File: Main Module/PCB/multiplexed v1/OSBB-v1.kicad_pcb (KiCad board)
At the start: 2 copper layers, 85.6 x 49.8 mm, 42 parts, among them P1 AUX 1-3, P14 EXTRA Pins, P2 Wire to Teensy VUSB, P3 +3.3V, P4 Pit Limiter, P5 Encoders, P6 BTN 1-32, Q1 NPN, Q2 NPN, Q3 NPN, Q4 NPN, U1 74HC4051, U2 74HC4051, U3 74HC4051, U4 74HC4051, U5 Teensy3.2

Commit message: * RC5-dev joined missing ground traces for right side of board
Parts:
- removed the REF** at (190.8, 121.5)
- removed the REF** at (243.7, 125.5)
- P4: value Pit Limiter -> Pit
- moved C6 5.32 mm to (210.7, 125.9), turned to 270 degrees
- moved REF** 0.08 mm to (180.4, 121.7)
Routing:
- net Net-(R2-Pad1): track 20.1 -> 22.7 mm
- net GND: track 311.3 -> 313.4 mm, vias 7 -> 8
- net +3V3: track 311.1 -> 311.9 mm, vias 8 -> 10
- net Net-(R7-Pad1): track 25.2 -> 25.3 mm, vias 1 -> 2
- net Net-(U1-Pad3): vias 1 -> 0

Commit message: * PCB RC5-dev labels
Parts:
- removed the G*** at (179.6, 126.6)
- added G***: LOGO, MOBB-KiCad-Lib:OPEN_HW_LOGO_3MM, F.Cu at (179.8, 126.5)
- added REF***: OSHW-Logo_5.7x6mm_Copper, Symbols:OSHW-Logo_5.7x6mm_Copper, B.Cu at (181.1, 127.6)
- moved Q1 0.60 mm to (195.6, 140.5)
- moved Q2 0.58 mm to (201.2, 140.5)
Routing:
- net Net-(U4-Pad3): track 28.7 -> 26.5 mm, vias 3 -> 4
- net Net-(P6-Pad57): track 20.3 -> 19.0 mm
- net Net-(P1-Pad5): track 16.4 -> 17.5 mm
- net GND: track 313.4 -> 314.2 mm
- net Net-(P1-Pad1): track 24.7 -> 24.0 mm
- net Net-(P1-Pad3): track 14.2 -> 13.6 mm
- net Net-(Q2-Pad2): track 24.7 -> 24.1 mm
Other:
- board text added: "(c) 2016 Mirko Kaiser"
- board text added: "+"
- board text added: "-"
- board text added: "32"

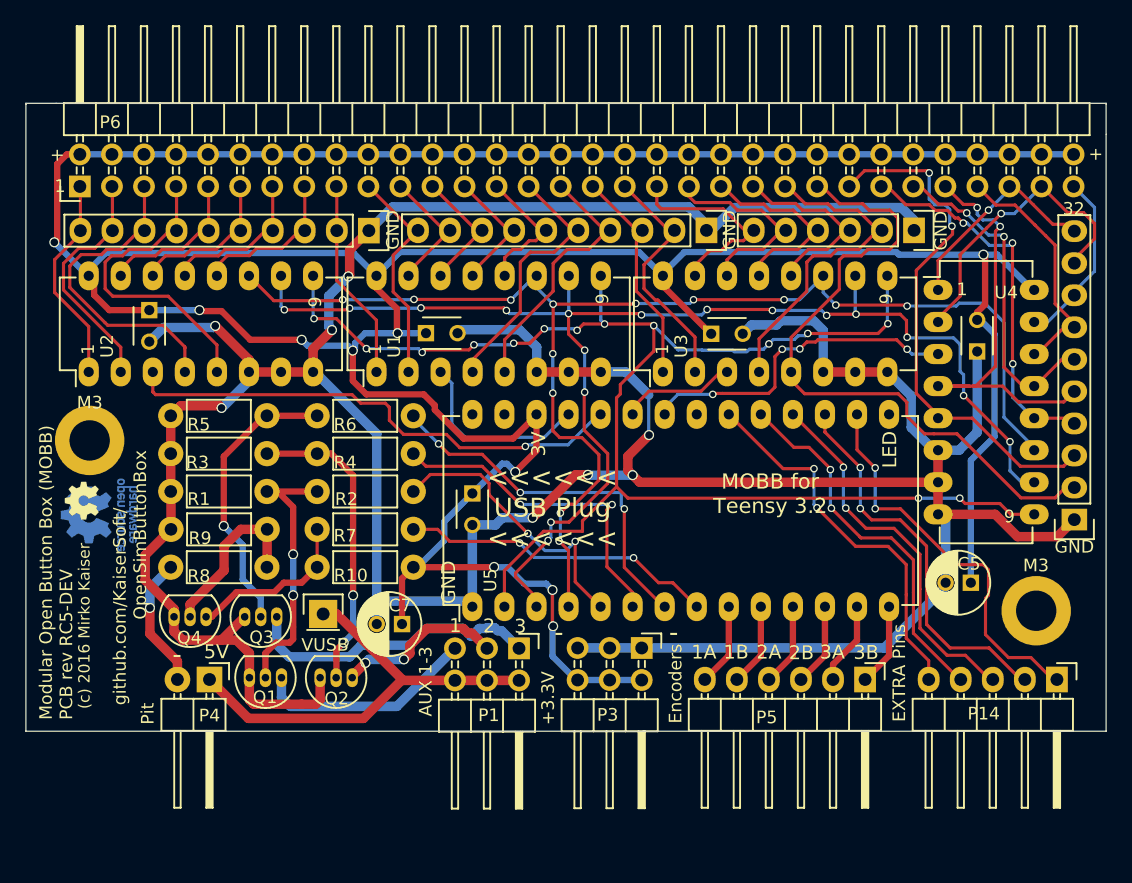
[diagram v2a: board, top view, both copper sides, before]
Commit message: * changed orientation of cap to give more room around screw * adjusted distance between lower pins (aux, 3v...) * more labels
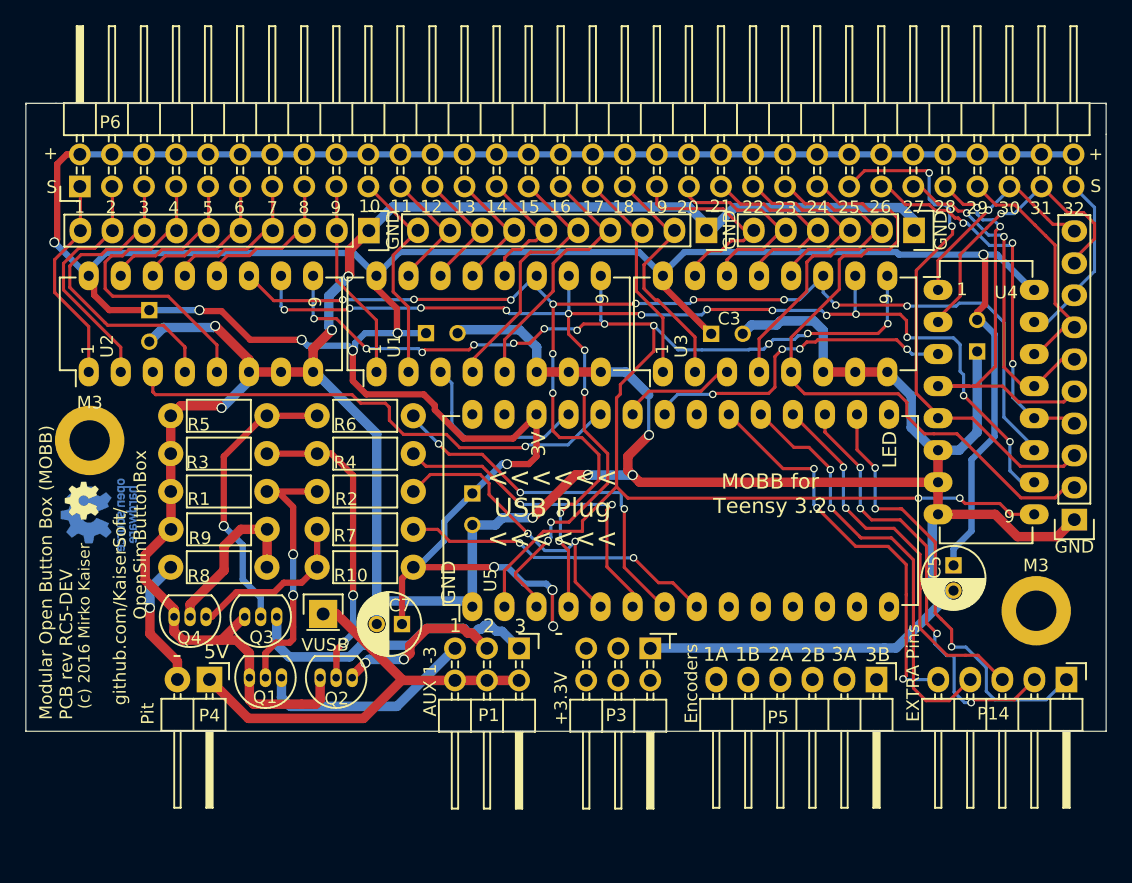
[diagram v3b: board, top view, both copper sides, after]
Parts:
- C1, C2, C3, C4, C6: moved to B.Cu
- moved C5 1.94 mm to (248.8, 131.6), turned to 270 degrees
- moved P5 0.91 mm to (242.7, 140.7)
- moved P14 0.76 mm to (257.8, 140.7)
- moved P3 0.68 mm to (224.8, 138.2)
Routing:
- net +3V3: track 311.9 -> 300.7 mm
- net Net-(P5-Pad6): track 6.56 -> 0.00 mm
- net Net-(P5-Pad5): track 6.56 -> 0.00 mm
- net Net-(P5-Pad4): track 6.56 -> 0.00 mm
- net Net-(P5-Pad1): track 6.56 -> 0.00 mm
- net Net-(P5-Pad2): track 6.56 -> 0.00 mm
- net Net-(P5-Pad3): track 6.56 -> 0.00 mm
- net Net-(P14-Pad4): track 29.7 -> 34.4 mm
- net Net-(P14-Pad2): track 30.9 -> 35.5 mm, vias 2 -> 4
- net GND: track 314.2 -> 310.2 mm
- net Net-(P14-Pad1): track 31.8 -> 35.7 mm, vias 2 -> 3
- net Net-(P14-Pad5): track 30.8 -> 33.0 mm, vias 2 -> 3
- net Net-(P14-Pad3): track 29.9 -> 30.6 mm
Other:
- board text added: "10"
- board text added: "11"
- board text added: "12"
- board text added: "13"
- board text added: "14"
- board text added: "15"
- board text added: "16"
- board text added: "17"
- board text added: "18"
- board text added: "19"
- board text added: "20"
- board text added: "21"
- board text added: "22"
- board text added: "23"
- board text added: "24"
- board text added: "25"
- board text added: "26"
- board text added: "27"
- board text added: "28"
- board text added: "29"
- board text added: "30"
- board text added: "31"
- board text added: "4"
- board text added: "5"
- board text added: "6"
- board text added: "7"
- board text added: "8"
- board text added: "S"

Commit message: * fixed missing tracks from last release
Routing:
- net +3V3: track 300.7 -> 311.8 mm
- net Net-(P5-Pad6): track 0.00 -> 6.19 mm
- net Net-(P5-Pad5): track 0.00 -> 6.19 mm
- net Net-(P5-Pad4): track 0.00 -> 6.19 mm
- net Net-(P5-Pad2): track 0.00 -> 6.19 mm
- net Net-(P5-Pad1): track 0.00 -> 6.19 mm
- net Net-(P5-Pad3): track 0.00 -> 6.19 mm
- net GND: track 310.2 -> 315.6 mm
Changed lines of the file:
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@@
   (general
     (links 194)
-    (no_connects 11)
+    (no_connects 0)
     (area 175.269999 88.074999 261.407144 151.803575)
     (thickness 1.6)
     (drawings 97)
-    (tracks 1131)
+    (tracks 1158)
     (zones 0)
     (modules 41)
@@
   (segment (start 195.575 142.1) (end 195.575 140.525) (width 0.75) (layer B.Cu) (net 4))
   (segment (start 196.275 142.8) (end 195.575 142.1) (width 0.75) (layer B.Cu) (net 4))
-  (segment (start 217.1 136.45) (end 217.2 136.45) (width 0.5) (layer B.Cu) (net 5))
+  (segment (start 222.26 140.74) (end 224.8 140.74) (width 0.5) (layer B.Cu) (net 5) (status C00000))
+  (segment (start 219.72 140.74) (end 222.26 140.74) (width 0.5) (layer B.Cu) (net 5) (status C00000))
+  (segment (start 217.1 136.45) (end 217.1 139.3) (width 0.5) (layer B.Cu) (net 5))
   (via (at 217.1 136.45) (size 0.8) (drill 0.6) (layers F.Cu B.Cu) (net 5))
+  (segment (start 217.2 136.45) (end 217.1 136.45) (width 0.5) (layer B.Cu) (net 5))
+  (segment (start 218.54 140.74) (end 219.72 140.74) (width 0.5) (layer B.Cu) (net 5) (status 800000))
+  (segment (start 217.1 139.3) (end 218.54 140.74) (width 0.5) (layer B.Cu) (net 5))
   (segment (start 250.25 123.25) (end 252.075 121.425) (width 0.5) (layer B.Cu) (net 5))
   (segment (start 252.075 113.3) (end 252.075 121.425) (width 0.5) (layer B.Cu) (net 5))
@@
   (segment (start 255.8 99.06) (end 253.26 99.06) (width 0.5) (layer B.Cu) (net 5))
   (segment (start 258.61 99.06) (end 258.34 99.06) (width 0.5) (layer B.Cu) (net 5))
-  (segment (start 225.08 138.17) (end 243.33 138.17) (width 0.75) (layer B.Cu) (net 6))
+  (segment (start 222.26 138.2) (end 219.72 138.2) (width 0.75) (layer B.Cu) (net 6) (status C00000))
+  (segment (start 224.8 138.2) (end 222.26 138.2) (width 0.75) (layer B.Cu) (net 6) (status C00000))
+  (segment (start 243.35 138.17) (end 224.83 138.17) (width 0.75) (layer B.Cu) (net 6) (status 800000))
+  (segment (start 224.83 138.17) (end 224.8 138.2) (width 0.75) (layer B.Cu) (net 6) (status C00000))
   (segment (start 244.28 138.17) (end 248.825 133.625) (width 0.75) (layer B.Cu) (net 6))
-  (segment (start 243.33 138.17) (end 244.28 138.17) (width 0.75) (layer B.Cu) (net 6))
+  (segment (start 243.33 138.17) (end 243.35 138.17) (width 0.75) (layer B.Cu) (net 6))
+  (segment (start 243.35 138.17) (end 244.28 138.17) (width 0.75) (layer B.Cu) (net 6))
   (segment (start 225.08 138.17) (end 225.05 138.2) (width 0.75) (layer B.Cu) (net 6))
   (segment (start 248.825 133.625) (end 247.875 133.625) (width 0.75) (layer B.Cu) (net 6))
@@
   (segment (start 185.15 137.05) (end 187.33 139.23) (width 0.75) (layer F.Cu) (net 7))
   (segment (start 187.33 139.23) (end 187.33 140.67) (width 0.75) (layer F.Cu) (net 7))
+  (segment (start 243.72 134.9) (end 243.72 137.605) (width 0.5) (layer F.Cu) (net 8) (status 400000))
+  (segment (start 242.725 138.6) (end 242.725 140.675) (width 0.5) (layer F.Cu) (net 8) (status 800000))
+  (segment (start 243.72 137.605) (end 242.725 138.6) (width 0.5) (layer F.Cu) (net 8))
+  (segment (start 241.18 134.9) (end 241.18 137.195) (width 0.5) (layer F.Cu) (net 9) (status 400000))
+  (segment (start 240.185 138.19) (end 240.185 140.675) (width 0.5) (layer F.Cu) (net 9) (status 800000))
+  (segment (start 241.18 137.195) (end 240.185 138.19) (width 0.5) (layer F.Cu) (net 9))
+  (segment (start 238.64 134.9) (end 238.64 137.635) (width 0.5) (layer F.Cu) (net 10) (status 400000))
+  (segment (start 237.645 138.63) (end 237.645 140.675) (width 0.5) (layer F.Cu) (net 10) (status 800000))
+  (segment (start 238.64 137.635) (end 237.645 138.63) (width 0.5) (layer F.Cu) (net 10))
+  (segment (start 236.1 134.9) (end 236.1 137.85) (width 0.5) (layer F.Cu) (net 11) (status 400000))
+  (segment (start 235.105 138.845) (end 235.105 140.675) (width 0.5) (layer F.Cu) (net 11) (status 800000))
+  (segment (start 236.1 137.85) (end 235.105 138.845) (width 0.5) (layer F.Cu) (net 11))
+  (segment (start 233.56 134.9) (end 233.56 138.04) (width 0.5) (layer F.Cu) (net 12) (status 400000))
+  (segment (start 232.565 139.035) (end 232.565 140.675) (width 0.5) (layer F.Cu) (net 12) (status 800000))
+  (segment (start 233.56 138.04) (end 232.565 139.035) (width 0.5) (layer F.Cu) (net 12))
+  (segment (start 231.02 134.9) (end 231.02 138.13) (width 0.5) (layer F.Cu) (net 13) (status 400000))
+  (segment (start 230.025 139.125) (end 230.025 140.675) (width 0.5) (layer F.Cu) (net 13) (status 800000))
+  (segment (start 231.02 138.13) (end 230.025 139.125) (width 0.5) (layer F.Cu) (net 13))
   (segment (start 179.64 105.1) (end 179.64 101.64) (width 0.25) (layer F.Cu) (net 14))
   (segment (start 179.64 101.64) (end 179.6 101.6) (width 0.25) (layer F.Cu) (net 14))

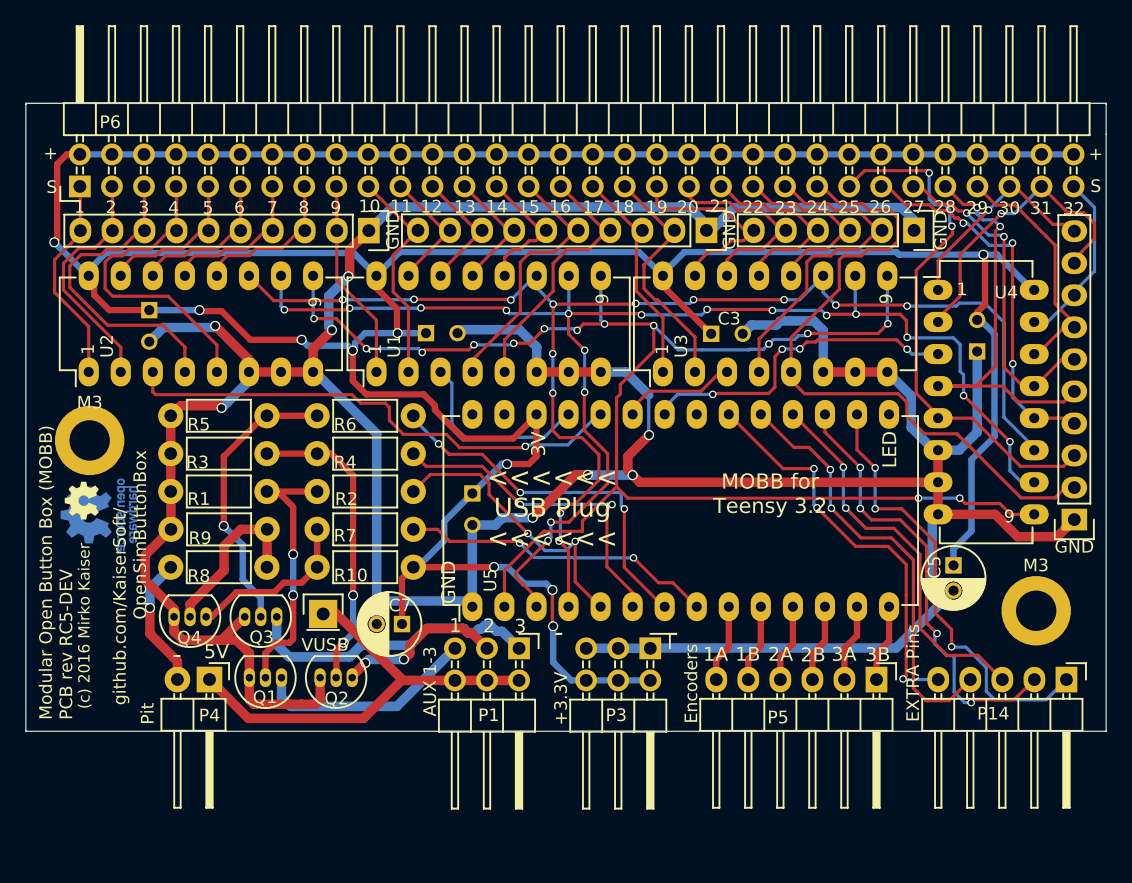
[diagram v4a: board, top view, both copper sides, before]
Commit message: * flooded with GND * added vias
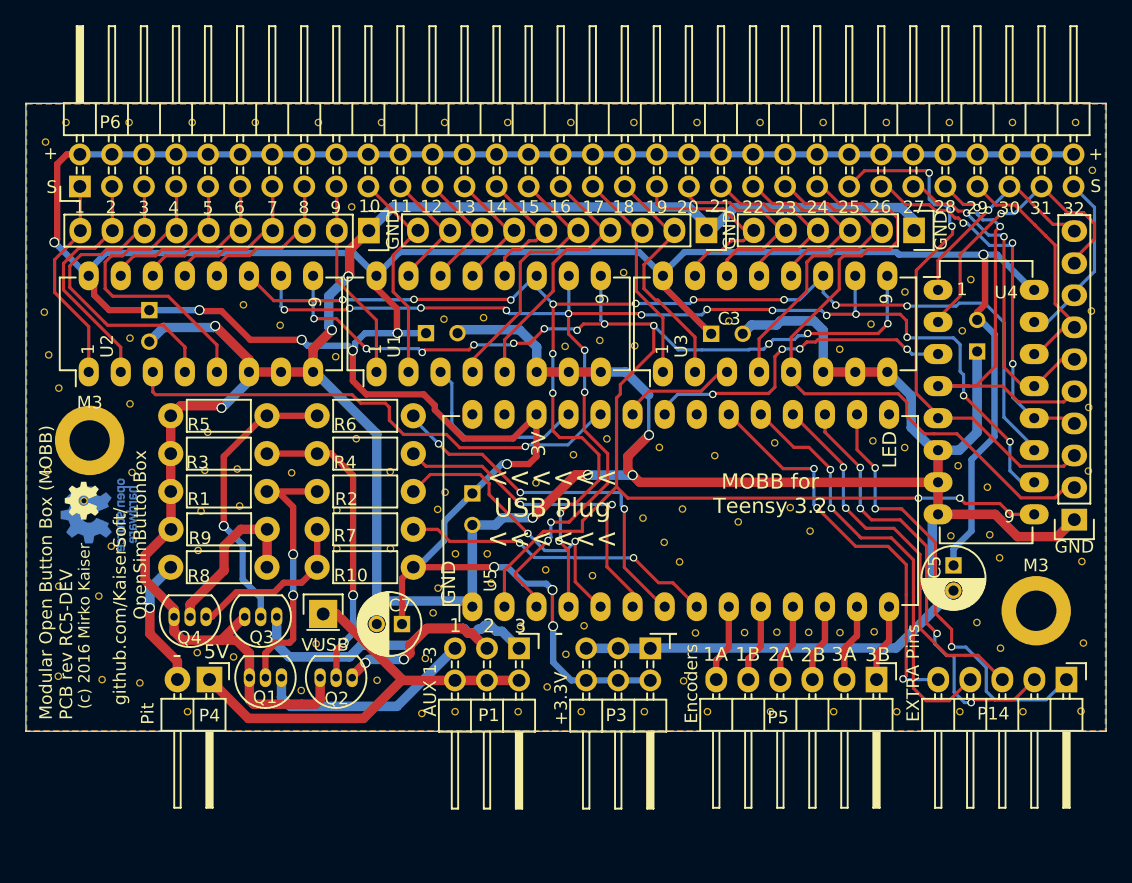
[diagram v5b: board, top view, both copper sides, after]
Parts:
- added Ref**: Val**, MOBB-KiCad-Lib:VIA-W0.6mm-H0.4mm, F.Cu at (258.9, 143.2)
- added Ref**: Val**, MOBB-KiCad-Lib:VIA-W0.6mm-H0.4mm, F.Cu at (214.3, 143.2)
- added Ref**: Val**, MOBB-KiCad-Lib:VIA-W0.6mm-H0.4mm, F.Cu at (184.3, 140.9)
- added Ref**: Val**, MOBB-KiCad-Lib:VIA-W0.6mm-H0.4mm, F.Cu at (188.1, 143.2)
- added Ref**: Val**, MOBB-KiCad-Lib:VIA-W0.6mm-H0.4mm, F.Cu at (188.9, 138.5)
- added Ref**: Val**, MOBB-KiCad-Lib:VIA-W0.6mm-H0.4mm, F.Cu at (191.8, 138.9)
- added Ref**: Val**, MOBB-KiCad-Lib:VIA-W0.6mm-H0.4mm, F.Cu at (198.3, 137.8)
- added Ref**: Val**, MOBB-KiCad-Lib:VIA-W0.6mm-H0.4mm, F.Cu at (197.1, 141.5)
- added Ref**: Val**, MOBB-KiCad-Lib:VIA-W0.6mm-H0.4mm, F.Cu at (206.7, 143.4)
- added Ref**: Val**, MOBB-KiCad-Lib:VIA-W0.6mm-H0.4mm, F.Cu at (209.3, 143.2)
- added Ref**: Val**, MOBB-KiCad-Lib:VIA-W0.6mm-H0.4mm, F.Cu at (214.5, 136.4)
- added Ref**: Val**, MOBB-KiCad-Lib:VIA-W0.6mm-H0.4mm, F.Cu at (219.6, 136.4)
- added Ref**: Val**, MOBB-KiCad-Lib:VIA-W0.6mm-H0.4mm, F.Cu at (178.5, 96.5)
- added Ref**: Val**, MOBB-KiCad-Lib:VIA-W0.6mm-H0.4mm, F.Cu at (218.1, 138.7)
- added Ref**: Val**, MOBB-KiCad-Lib:VIA-W0.6mm-H0.4mm, F.Cu at (216.6, 141.3)
- added Ref**: Val**, MOBB-KiCad-Lib:VIA-W0.6mm-H0.4mm, F.Cu at (228.4, 137.0)
- added Ref**: Val**, MOBB-KiCad-Lib:VIA-W0.6mm-H0.4mm, F.Cu at (227.4, 140.8)
- added Ref**: Val**, MOBB-KiCad-Lib:VIA-W0.6mm-H0.4mm, F.Cu at (252.6, 138.2)
- added Ref**: Val**, MOBB-KiCad-Lib:VIA-W0.6mm-H0.4mm, F.Cu at (250.7, 136.2)
- added Ref**: Val**, MOBB-KiCad-Lib:VIA-W0.6mm-H0.4mm, F.Cu at (259.1, 137.8)
- added Ref**: Val**, MOBB-KiCad-Lib:VIA-W0.6mm-H0.4mm, F.Cu at (259.0, 131.3)
- added Ref**: Val**, MOBB-KiCad-Lib:VIA-W0.6mm-H0.4mm, F.Cu at (252.5, 131.0)
- added Ref**: Val**, MOBB-KiCad-Lib:VIA-W0.6mm-H0.4mm, F.Cu at (251.7, 129.2)
- added Ref**: Val**, MOBB-KiCad-Lib:VIA-W0.6mm-H0.4mm, F.Cu at (183.5, 96.5)
- added Ref**: Val**, MOBB-KiCad-Lib:VIA-W0.6mm-H0.4mm, F.Cu at (248.6, 129.3)
- added Ref**: Val**, MOBB-KiCad-Lib:VIA-W0.6mm-H0.4mm, F.Cu at (235.9, 127.0)
- added Ref**: Val**, MOBB-KiCad-Lib:VIA-W0.6mm-H0.4mm, F.Cu at (237.5, 128.9)
- added Ref**: Val**, MOBB-KiCad-Lib:VIA-W0.6mm-H0.4mm, F.Cu at (231.8, 128.2)
- added Ref**: Val**, MOBB-KiCad-Lib:VIA-W0.6mm-H0.4mm, F.Cu at (227.3, 127.2)
- added Ref**: Val**, MOBB-KiCad-Lib:VIA-W0.6mm-H0.4mm, F.Cu at (227.1, 131.3)
- added Ref**: Val**, MOBB-KiCad-Lib:VIA-W0.6mm-H0.4mm, F.Cu at (225.9, 129.8)
- added Ref**: Val**, MOBB-KiCad-Lib:VIA-W0.6mm-H0.4mm, F.Cu at (224.2, 127.9)
- added Ref**: Val**, MOBB-KiCad-Lib:VIA-W0.6mm-H0.4mm, F.Cu at (188.5, 96.5)
- added Ref**: Val**, MOBB-KiCad-Lib:VIA-W0.6mm-H0.4mm, F.Cu at (193.5, 96.5)
- added Ref**: Val**, MOBB-KiCad-Lib:VIA-W0.6mm-H0.4mm, F.Cu at (198.5, 96.5)
- added Ref**: Val**, MOBB-KiCad-Lib:VIA-W0.6mm-H0.4mm, F.Cu at (203.5, 96.5)
- added Ref**: Val**, MOBB-KiCad-Lib:VIA-W0.6mm-H0.4mm, F.Cu at (208.5, 96.5)
- added Ref**: Val**, MOBB-KiCad-Lib:VIA-W0.6mm-H0.4mm, F.Cu at (213.5, 96.5)
- added Ref**: Val**, MOBB-KiCad-Lib:VIA-W0.6mm-H0.4mm, F.Cu at (218.5, 96.5)
- added Ref**: Val**, MOBB-KiCad-Lib:VIA-W0.6mm-H0.4mm, F.Cu at (254.3, 143.2)
- added Ref**: Val**, MOBB-KiCad-Lib:VIA-W0.6mm-H0.4mm, F.Cu at (223.5, 96.5)
- added Ref**: Val**, MOBB-KiCad-Lib:VIA-W0.6mm-H0.4mm, F.Cu at (228.5, 96.5)
- added Ref**: Val**, MOBB-KiCad-Lib:VIA-W0.6mm-H0.4mm, F.Cu at (233.5, 96.5)
- added Ref**: Val**, MOBB-KiCad-Lib:VIA-W0.6mm-H0.4mm, F.Cu at (238.5, 96.5)
- added Ref**: Val**, MOBB-KiCad-Lib:VIA-W0.6mm-H0.4mm, F.Cu at (243.5, 96.5)
- added Ref**: Val**, MOBB-KiCad-Lib:VIA-W0.6mm-H0.4mm, F.Cu at (248.5, 96.5)
- added Ref**: Val**, MOBB-KiCad-Lib:VIA-W0.6mm-H0.4mm, F.Cu at (253.5, 96.5)
- added Ref**: Val**, MOBB-KiCad-Lib:VIA-W0.6mm-H0.4mm, F.Cu at (245.0, 110.0)
- added Ref**: Val**, MOBB-KiCad-Lib:VIA-W0.6mm-H0.4mm, F.Cu at (222.7, 108.4)
- added Ref**: Val**, MOBB-KiCad-Lib:VIA-W0.6mm-H0.4mm, F.Cu at (200.0, 130.3)
- added Ref**: Val**, MOBB-KiCad-Lib:VIA-W0.6mm-H0.4mm, F.Cu at (249.3, 143.2)
- added Ref**: Val**, MOBB-KiCad-Lib:VIA-W0.6mm-H0.4mm, F.Cu at (200.0, 127.3)
- added Ref**: Val**, MOBB-KiCad-Lib:VIA-W0.6mm-H0.4mm, F.Cu at (196.4, 124.3)
- added Ref**: Val**, MOBB-KiCad-Lib:VIA-W0.6mm-H0.4mm, F.Cu at (192.1, 124.0)
- added Ref**: Val**, MOBB-KiCad-Lib:VIA-W0.6mm-H0.4mm, F.Cu at (192.3, 126.9)
- added Ref**: Val**, MOBB-KiCad-Lib:VIA-W0.6mm-H0.4mm, F.Cu at (207.0, 139.0)
- added Ref**: Val**, MOBB-KiCad-Lib:VIA-W0.6mm-H0.4mm, F.Cu at (203.2, 140.7)
- added Ref**: Val**, MOBB-KiCad-Lib:VIA-W0.6mm-H0.4mm, F.Cu at (242.5, 136.9)
- added Ref**: Val**, MOBB-KiCad-Lib:VIA-W0.6mm-H0.4mm, F.Cu at (239.8, 136.9)
- added Ref**: Val**, MOBB-KiCad-Lib:VIA-W0.6mm-H0.4mm, F.Cu at (237.3, 136.9)
- added Ref**: Val**, MOBB-KiCad-Lib:VIA-W0.6mm-H0.4mm, F.Cu at (234.8, 136.9)
- added Ref**: Val**, MOBB-KiCad-Lib:VIA-W0.6mm-H0.4mm, F.Cu at (244.3, 143.2)
- added Ref**: Val**, MOBB-KiCad-Lib:VIA-W0.6mm-H0.4mm, F.Cu at (232.3, 136.9)
- added Ref**: Val**, MOBB-KiCad-Lib:VIA-W0.6mm-H0.4mm, F.Cu at (245.0, 122.3)
- added Ref**: Val**, MOBB-KiCad-Lib:VIA-W0.6mm-H0.4mm, F.Cu at (242.4, 121.8)
- added Ref**: Val**, MOBB-KiCad-Lib:VIA-W0.6mm-H0.4mm, F.Cu at (201.1, 103.2)
- added Ref**: Val**, MOBB-KiCad-Lib:VIA-W0.6mm-H0.4mm, F.Cu at (221.4, 121.6)
- added Ref**: Val**, MOBB-KiCad-Lib:VIA-W0.6mm-H0.4mm, F.Cu at (234.7, 121.9)
- added Ref**: Val**, MOBB-KiCad-Lib:VIA-W0.6mm-H0.4mm, F.Cu at (249.2, 123.7)
- added Ref**: Val**, MOBB-KiCad-Lib:VIA-W0.6mm-H0.4mm, F.Cu at (251.5, 125.4)
- added Ref**: Val**, MOBB-KiCad-Lib:VIA-W0.6mm-H0.4mm, F.Cu at (259.5, 124.2)
- added Ref**: Val**, MOBB-KiCad-Lib:VIA-W0.6mm-H0.4mm, F.Cu at (259.5, 119.1)
- added Ref**: Val**, MOBB-KiCad-Lib:VIA-W0.6mm-H0.4mm, F.Cu at (239.3, 143.2)
- added Ref**: Val**, MOBB-KiCad-Lib:VIA-W0.6mm-H0.4mm, F.Cu at (259.8, 111.5)
- added Ref**: Val**, MOBB-KiCad-Lib:VIA-W0.6mm-H0.4mm, F.Cu at (250.2, 109.0)
- added Ref**: Val**, MOBB-KiCad-Lib:VIA-W0.6mm-H0.4mm, F.Cu at (249.5, 113.0)
- added Ref**: Val**, MOBB-KiCad-Lib:VIA-W0.6mm-H0.4mm, F.Cu at (242.3, 112.5)
- added Ref**: Val**, MOBB-KiCad-Lib:VIA-W0.6mm-H0.4mm, F.Cu at (239.8, 114.5)
- added Ref**: Val**, MOBB-KiCad-Lib:VIA-W0.6mm-H0.4mm, F.Cu at (231.0, 112.3)
- added Ref**: Val**, MOBB-KiCad-Lib:VIA-W0.6mm-H0.4mm, F.Cu at (223.6, 114.2)
- added Ref**: Val**, MOBB-KiCad-Lib:VIA-W0.6mm-H0.4mm, F.Cu at (220.8, 113.8)
- added Ref**: Val**, MOBB-KiCad-Lib:VIA-W0.6mm-H0.4mm, F.Cu at (218.1, 114.3)
- added Ref**: Val**, MOBB-KiCad-Lib:VIA-W0.6mm-H0.4mm, F.Cu at (208.4, 112.1)
- added Ref**: Val**, MOBB-KiCad-Lib:VIA-W0.6mm-H0.4mm, F.Cu at (234.3, 143.2)
- added Ref**: Val**, MOBB-KiCad-Lib:VIA-W0.6mm-H0.4mm, F.Cu at (211.6, 112.0)
- added Ref**: Val**, MOBB-KiCad-Lib:VIA-W0.6mm-H0.4mm, F.Cu at (199.9, 115.1)
- added Ref**: Val**, MOBB-KiCad-Lib:VIA-W0.6mm-H0.4mm, F.Cu at (195.5, 112.6)
- added Ref**: Val**, MOBB-KiCad-Lib:VIA-W0.6mm-H0.4mm, F.Cu at (192.6, 111.0)
- added Ref**: Val**, MOBB-KiCad-Lib:VIA-W0.6mm-H0.4mm, F.Cu at (183.6, 113.6)
- added Ref**: Val**, MOBB-KiCad-Lib:VIA-W0.6mm-H0.4mm, F.Cu at (183.7, 124.3)
- added Ref**: Val**, MOBB-KiCad-Lib:VIA-W0.6mm-H0.4mm, F.Cu at (183.6, 118.8)
- added Ref**: Val**, MOBB-KiCad-Lib:VIA-W0.6mm-H0.4mm, F.Cu at (177.9, 117.6)
- added Ref**: Val**, MOBB-KiCad-Lib:VIA-W0.6mm-H0.4mm, F.Cu at (189.7, 121.1)
- added Ref**: Val**, MOBB-KiCad-Lib:VIA-W0.6mm-H0.4mm, F.Cu at (189.5, 124.1)
- added Ref**: Val**, MOBB-KiCad-Lib:VIA-W0.6mm-H0.4mm, F.Cu at (229.3, 143.2)
- added Ref**: Val**, MOBB-KiCad-Lib:VIA-W0.6mm-H0.4mm, F.Cu at (189.2, 127.3)
- added Ref**: Val**, MOBB-KiCad-Lib:VIA-W0.6mm-H0.4mm, F.Cu at (189.0, 130.4)
- added Ref**: Val**, MOBB-KiCad-Lib:VIA-W0.6mm-H0.4mm, F.Cu at (204.2, 130.3)
- added Ref**: Val**, MOBB-KiCad-Lib:VIA-W0.6mm-H0.4mm, F.Cu at (204.2, 124.2)
- added Ref**: Val**, MOBB-KiCad-Lib:VIA-W0.6mm-H0.4mm, F.Cu at (201.5, 121.6)
- added Ref**: Val**, MOBB-KiCad-Lib:VIA-W0.6mm-H0.4mm, F.Cu at (220.2, 132.4)
- added Ref**: Val**, MOBB-KiCad-Lib:VIA-W0.6mm-H0.4mm, F.Cu at (216.5, 132.0)
- added Ref**: Val**, MOBB-KiCad-Lib:VIA-W0.6mm-H0.4mm, F.Cu at (209.4, 130.7)
- added Ref**: Val**, MOBB-KiCad-Lib:VIA-W0.6mm-H0.4mm, F.Cu at (211.9, 130.7)
- added Ref**: Val**, MOBB-KiCad-Lib:VIA-W0.6mm-H0.4mm, F.Cu at (212.2, 133.0)
- added Ref**: Val**, MOBB-KiCad-Lib:VIA-W0.6mm-H0.4mm, F.Cu at (224.3, 143.2)
- added Ref**: Val**, MOBB-KiCad-Lib:VIA-W0.6mm-H0.4mm, F.Cu at (207.6, 135.4)
- added Ref**: Val**, MOBB-KiCad-Lib:VIA-W0.6mm-H0.4mm, F.Cu at (208.0, 133.4)
- added Ref**: Val**, MOBB-KiCad-Lib:VIA-W0.6mm-H0.4mm, F.Cu at (207.9, 127.2)
- added Ref**: Val**, MOBB-KiCad-Lib:VIA-W0.6mm-H0.4mm, F.Cu at (208.5, 125.8)
- added Ref**: Val**, MOBB-KiCad-Lib:VIA-W0.6mm-H0.4mm, F.Cu at (215.7, 125.1)
- added Ref**: Val**, MOBB-KiCad-Lib:VIA-W0.6mm-H0.4mm, F.Cu at (218.7, 122.9)
- added Ref**: Val**, MOBB-KiCad-Lib:VIA-W0.6mm-H0.4mm, F.Cu at (229.9, 122.9)
- added Ref**: Val**, MOBB-KiCad-Lib:VIA-W0.6mm-H0.4mm, F.Cu at (225.5, 122.3)
- added Ref**: Val**, MOBB-KiCad-Lib:VIA-W0.6mm-H0.4mm, F.Cu at (259.8, 100.3)
- added Ref**: Val**, MOBB-KiCad-Lib:VIA-W0.6mm-H0.4mm, F.Cu at (258.5, 96.5)
- added Ref**: Val**, MOBB-KiCad-Lib:VIA-W0.6mm-H0.4mm, F.Cu at (219.3, 143.2)
- added Ref**: Val**, MOBB-KiCad-Lib:VIA-W0.6mm-H0.4mm, F.Cu at (176.9, 98.1)
- added Ref**: Val**, MOBB-KiCad-Lib:VIA-W0.6mm-H0.4mm, F.Cu at (176.8, 111.6)
- added Ref**: Val**, MOBB-KiCad-Lib:VIA-W0.6mm-H0.4mm, F.Cu at (177.1, 115.0)
- added Ref**: Val**, MOBB-KiCad-Lib:VIA-W0.6mm-H0.4mm, F.Cu at (177.0, 124.1)
- added Ref**: Val**, MOBB-KiCad-Lib:VIA-W0.6mm-H0.4mm, F.Cu at (179.9, 126.5)
- added Ref**: Val**, MOBB-KiCad-Lib:VIA-W0.6mm-H0.4mm, F.Cu at (182.1, 130.1)
- added Ref**: Val**, MOBB-KiCad-Lib:VIA-W0.6mm-H0.4mm, F.Cu at (181.4, 140.7)
- added Ref**: Val**, MOBB-KiCad-Lib:VIA-W0.6mm-H0.4mm, F.Cu at (181.1, 134.1)
- added Ref**: Val**, MOBB-KiCad-Lib:VIA-W0.6mm-H0.4mm, F.Cu at (177.9, 133.3)
- added Ref**: Val**, MOBB-KiCad-Lib:VIA-W0.6mm-H0.4mm, F.Cu at (177.9, 140.4)
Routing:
- added copper zone on B.Cu, net GND
- added copper zone on F.Cu, net GND
